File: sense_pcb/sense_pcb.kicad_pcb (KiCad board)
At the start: 2 copper layers, 31 parts, among them J1 Conn_02x06_Odd_Even, U1 DRV5053VAQDBZR, U10 DRV5053VAQDBZR, U11 DRV5053VAQDBZR, U12 DRV5053VAQDBZR, U13 DRV5053VAQDBZR, U14 4051, U15 DRV5053VAQDBZR, U16 DRV5053VAQDBZR, U17 DRV5053VAQDBZR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

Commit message: IC layout done
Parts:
- added J10, J11, J9: TEST_1P, SMD_Packages:1Pin, F.Cu at (226.6, 81.8)
- added J2: TEST_1P, SMD_Packages:1Pin, F.Cu at (241.1, 103.3)
- added J3: TEST_1P, SMD_Packages:1Pin, F.Cu at (240.7, 92.7)
- added J4: TEST_1P, SMD_Packages:1Pin, F.Cu at (216.1, 101.0)
- added J5: TEST_1P, SMD_Packages:1Pin, F.Cu at (208.3, 98.4)
- added J6: TEST_1P, SMD_Packages:1Pin, F.Cu at (225.4, 94.7)
- added J7: TEST_1P, SMD_Packages:1Pin, F.Cu at (233.1, 99.4)
- added J8: TEST_1P, SMD_Packages:1Pin, F.Cu at (252.2, 93.9)
- J1: value Conn_02x06_Odd_Even -> TEST_1P; footprint Pin_Headers:Pin_Header_Straight_2x06_Pitch2.54mm -> SMD_Packages:1Pin
- moved U21 112.4 mm to (258.7, 83.0), turned to 15 degrees
- moved U20 112.2 mm to (259.8, 91.3)
- moved U22 111.1 mm to (255.5, 75.2), turned to 30 degrees
- moved U19 110.4 mm to (258.7, 99.7), turned to 345 degrees
- moved U27 108.2 mm to (250.4, 68.5), turned to 45 degrees
- moved U8 107.0 mm to (255.5, 107.4), turned to 330 degrees
- moved U25 103.9 mm to (243.7, 63.4), turned to 60 degrees
- moved U23 102.9 mm to (248.2, 79.4), turned to 210 degrees
- moved U6 102.3 mm to (250.4, 114.1), turned to 315 degrees
- moved U24 98.2 mm to (235.9, 60.2), turned to 75 degrees
- moved U7 96.2 mm to (243.7, 119.3), turned to 300 degrees
- moved C2 95.8 mm to (241.7, 83.1), turned to 300 degrees
- moved U26 91.4 mm to (227.5, 59.0), turned to 90 degrees
- moved J1 89.2 mm to (237.1, 115.7), turned to 90 degrees
- moved U9 89.1 mm to (235.9, 122.5), turned to 285 degrees
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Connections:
- U14 pad 10: Net-(J1-Pad10) -> Net-(J10-Pad1)
- U14 pad 11: Net-(J1-Pad9) -> Net-(J3-Pad1)
- U14 pad 3: Net-(J1-Pad4) -> Net-(J9-Pad1)
- U14 pad 6: Net-(J1-Pad5) -> Net-(J4-Pad1)
- U14 pad 9: Net-(J1-Pad8) -> Net-(J7-Pad1)
- U23 pad 10: Net-(J1-Pad10) -> Net-(J10-Pad1)
- U23 pad 11: Net-(J1-Pad9) -> Net-(J3-Pad1)
- U23 pad 3: Net-(J1-Pad2) -> Net-(J11-Pad1)
- U23 pad 6: Net-(J1-Pad7) -> Net-(J5-Pad1)
- U23 pad 9: Net-(J1-Pad8) -> Net-(J7-Pad1)
- U5 pad 10: Net-(J1-Pad10) -> Net-(J10-Pad1)
- U5 pad 11: Net-(J1-Pad9) -> Net-(J3-Pad1)
- U5 pad 3: Net-(J1-Pad6) -> Net-(J8-Pad1)
- U5 pad 6: Net-(J1-Pad3) -> Net-(J2-Pad1)
- U5 pad 9: Net-(J1-Pad8) -> Net-(J7-Pad1)

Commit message: much smaller pads
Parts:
- J1, J10, J11, J2, J3, J4, J5, J6, J7, J8, J9: footprint SMD_Packages:1Pin -> Measurement_Points:Measurement_Point_Round-SMD-Pad_Small
- moved J5 33.3 mm to (240.3, 107.6)
- moved J10 29.8 mm to (251.0, 98.9)
- moved J9 28.2 mm to (244.1, 103.9)
- moved J11 26.8 mm to (246.3, 99.9)
- moved J4 26.5 mm to (240.2, 112.1)
- moved J6 24.2 mm to (245.3, 108.5)
- moved J7 16.5 mm to (249.1, 103.7)
- moved J3 16.3 mm to (253.9, 102.4)
- moved J8 14.9 mm to (250.2, 108.7)
- moved J2 11.2 mm to (244.8, 113.9)
- moved J1 2.10 mm to (238.0, 117.5)

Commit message: went over to Kicad 5.0, seems legit so far
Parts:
- removed C2, C3: C, Capacitors_SMD:C_1206_HandSoldering
- removed J10, J11, J8, J9: TEST_1P, Measurement_Points:Measurement_Point_Round-SMD-Pad_Small
- removed U10, U11, U12, U13, U15, U16, U17, U18, U19, U20, U21, U22, U24, U25, U26, U27: DRV5053VAQDBZR, digikey-footprints:SOT-23-3
- removed U14, U23: 4051, SMD_Packages:SO-16-N
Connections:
- J1 pad 1: VCC -> Net-(J1-Pad1)
- J2 pad 1: Net-(J2-Pad1) -> VCC
- J3 pad 1: Net-(J3-Pad1) -> GND
- J6 pad 1: GND -> Net-(J6-Pad1)
- U5 pad 10: Net-(J10-Pad1) -> Net-(J5-Pad1)
- U5 pad 11: Net-(J3-Pad1) -> Net-(J6-Pad1)
- U5 pad 3: Net-(J8-Pad1) -> Net-(J1-Pad1)
- U5 pad 6: Net-(J2-Pad1) -> Net-(J7-Pad1)
- U5 pad 9: Net-(J7-Pad1) -> Net-(J4-Pad1)

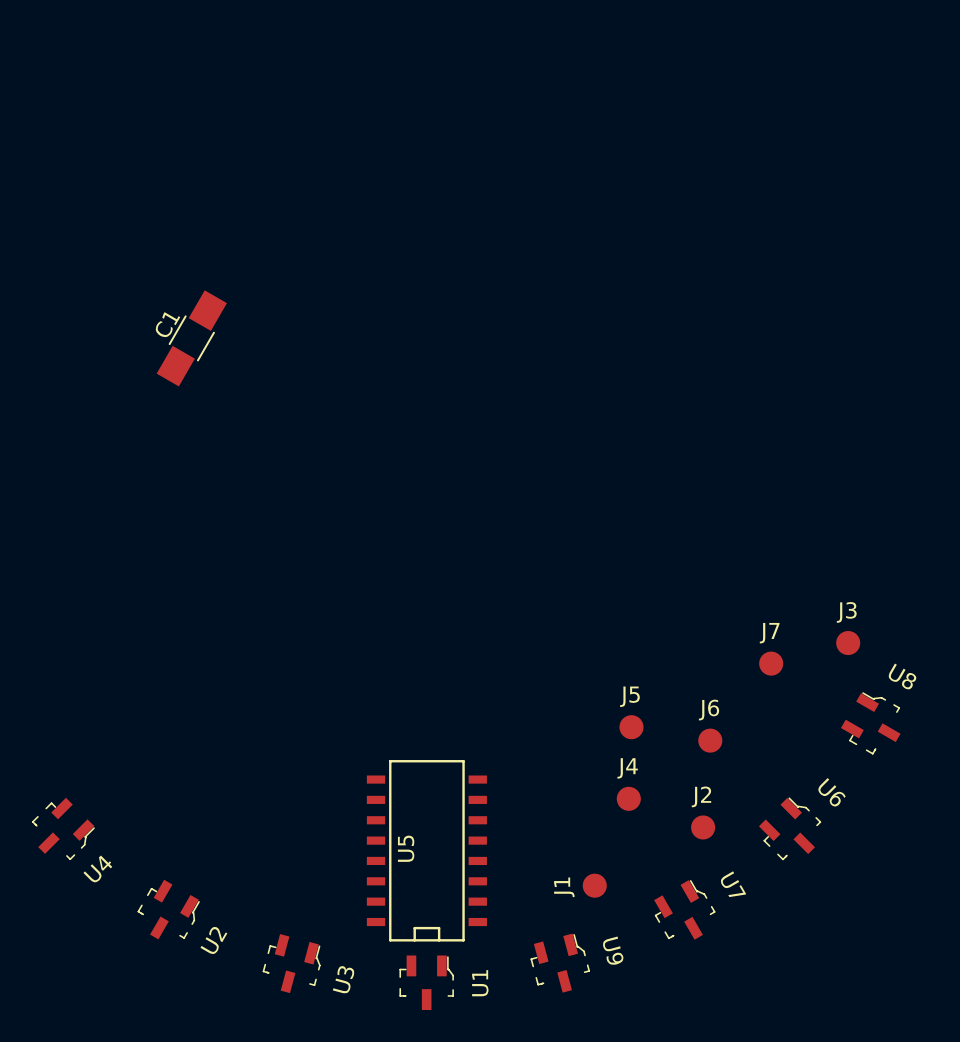
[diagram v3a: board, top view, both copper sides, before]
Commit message: layout with 8 sensors, no routing yet
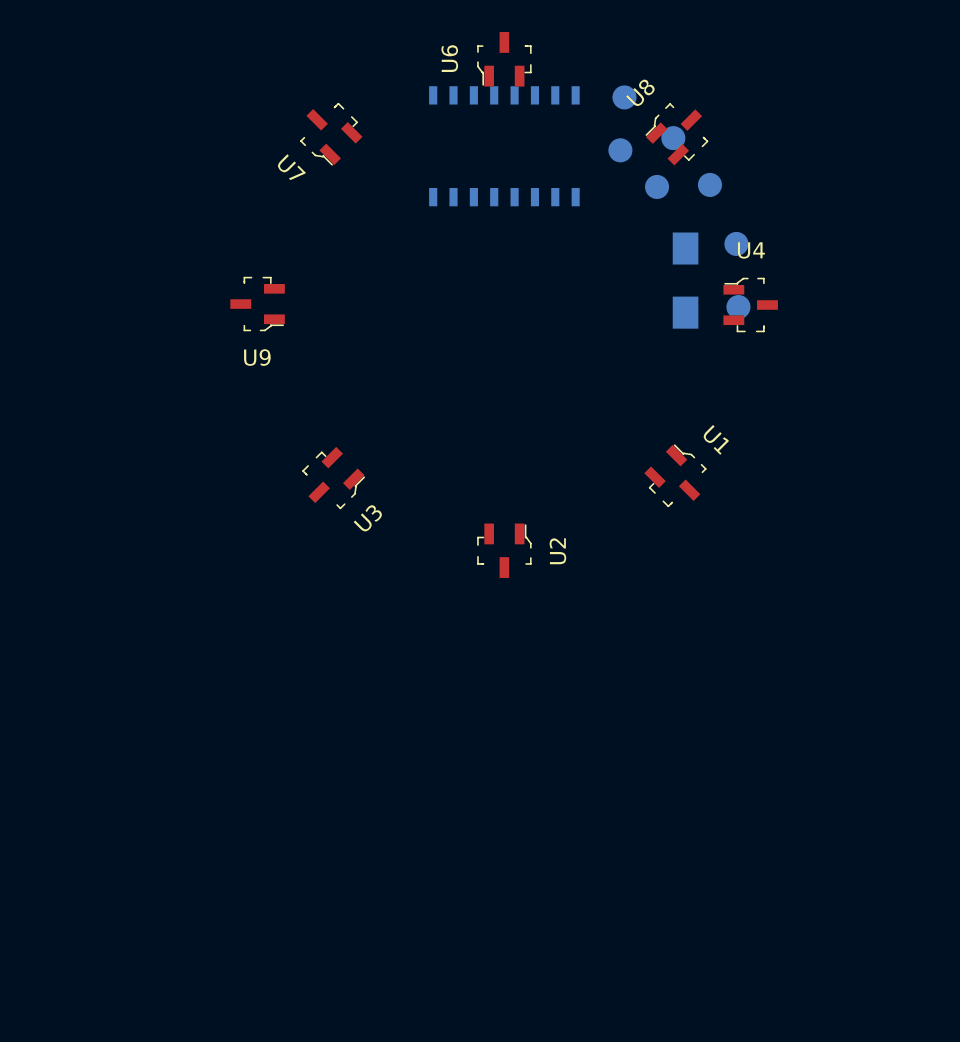
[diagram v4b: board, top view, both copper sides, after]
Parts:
- added G***: LOGO, graphics:layout.35mm, F.Cu at (232.4, 81.3)
- C1, J1, J2, J3, J4, J5, J6, J7, U5: moved to B.Cu
- moved U4 54.1 mm to (247.8, 81.3), turned to 0 degrees
- moved U7 53.6 mm to (221.5, 70.5), turned to 135 degrees
- moved U6 51.4 mm to (232.4, 65.9), turned to 90 degrees
- moved J1 46.9 mm to (243.0, 70.9), turned to 270 degrees
- moved U9 45.4 mm to (217.0, 81.2), turned to 180 degrees
- moved U5 44.2 mm to (232.4, 71.4), turned to 0 degrees
- moved U8 38.9 mm to (243.3, 70.5), turned to 45 degrees
- moved J4 38.6 mm to (245.2, 73.8)
- moved J6 37.3 mm to (239.6, 71.6)
- moved J7 36.5 mm to (239.9, 68.3)
- moved J2 36.5 mm to (246.9, 77.5)
- moved U1 35.2 mm to (243.2, 92.1), turned to 315 degrees
- moved J5 33.7 mm to (241.9, 73.9)
- moved C1 31.0 mm to (243.7, 79.8), turned to 270 degrees
- moved U2 30.9 mm to (232.4, 96.6), turned to 270 degrees
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
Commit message: routing complete
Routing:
- net VCC: track 0.00 -> 106.9 mm, vias 0 -> 3
- net GND: track 0.00 -> 97.9 mm, vias 0 -> 2
- net Net-(U2-Pad2): track 0.00 -> 29.7 mm, vias 0 -> 1
- net Net-(U1-Pad2): track 0.00 -> 29.3 mm, vias 0 -> 1
- net Net-(U4-Pad2): track 0.00 -> 22.6 mm, vias 0 -> 1
- net Net-(U3-Pad2): track 0.00 -> 20.7 mm, vias 0 -> 1
- net Net-(U5-Pad1): track 0.00 -> 15.9 mm, vias 0 -> 1
- net Net-(J1-Pad1): track 0.00 -> 14.4 mm
- net Net-(U5-Pad5): track 0.00 -> 12.4 mm, vias 0 -> 1
- net Net-(U5-Pad2): track 0.00 -> 10.6 mm, vias 0 -> 1
- net Net-(J4-Pad1): track 0.00 -> 9.50 mm
- net Net-(J5-Pad1): track 0.00 -> 8.09 mm
- net Net-(J6-Pad1): track 0.00 -> 8.02 mm
- net Net-(J7-Pad1): track 0.00 -> 7.51 mm
- net Net-(U5-Pad4): track 0.00 -> 5.20 mm, vias 0 -> 1

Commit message: adds v1 manufacturing files as sent to dirtypcbs.com
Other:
- board outline added: 35.6 x 35.6 mm
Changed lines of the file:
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@@
   (general
     (thickness 1.6)
-    (drawings 0)
+    (drawings 1)
     (tracks 159)
     (zones 0)
@@
       (xy -0.175598 -17.33005) (xy 0.565177 -17.32163)) (layer Eco1.User) (width 0.01))
   )
+  (gr_circle (center 232.41 81.28) (end 248.793 88.265) (layer Edge.Cuts) (width 0.2))
   (segment (start 233.36 95.563) (end 242.062 89.535) (width 0.45) (layer F.Cu) (net 1))
   (segment (start 242.062 89.535) (end 243.153827 90.680324) (width 0.45) (layer F.Cu) (net 1))

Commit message: adds sensor test
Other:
- outline, holes or cut-outs redrawn
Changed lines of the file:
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@@
-(kicad_pcb (version 20171130) (host pcbnew 5.0.2-bee76a0~70~ubuntu18.04.1)
+(kicad_pcb (version 4) (host pcbnew 4.0.7-e2-6376~58~ubuntu16.04.1)
   (general
+    (links 34)
+    (no_connects 0)
+    (area 210.093523 59.031523 254.692477 103.528476)
     (thickness 1.6)
-    (drawings 1)
+    (drawings 2)
     (tracks 159)
     (zones 0)
@@
   )
   (setup
-    (last_trace_width 0.45)
+    (last_trace_width 0.25)
     (user_trace_width 0.45)
     (user_trace_width 0.5)
@@
       (layerselection 0x00030_80000001)
       (usegerberextensions false)
-      (usegerberattributes false)
-      (usegerberadvancedattributes false)
-      (creategerberjobfile false)
       (excludeedgelayer true)
       (linewidth 0.100000)
@@
       (hpglpennumber 1)
       (hpglpenspeed 20)
-      (hpglpendiameter 15.000000)
+      (hpglpendiameter 15)
+      (hpglpenoverlay 2)
       (psnegative false)
       (psa4output false)
@@
     (at 232.41 81.28)
     (fp_text reference G*** (at 0 0) (layer F.SilkS) hide
-      (effects (font (size 1.524 1.524) (thickness 0.3)))
+      (effects (font (thickness 0.3)))
     )
     (fp_text value LOGO (at 0.75 0) (layer F.SilkS) hide
-      (effects (font (size 1.524 1.524) (thickness 0.3)))
+      (effects (font (thickness 0.3)))
     )
     (fp_poly (pts (xy 0.170867 -1.017051) (xy 0.328859 -0.977285) (xy 0.477313 -0.913687) (xy 0.613603 -0.828223)
@@
       (xy -0.175598 -17.33005) (xy 0.565177 -17.32163)) (layer Eco1.User) (width 0.01))
   )
+  (gr_circle (center 232.41508 81.28) (end 236.01172 82.45348) (layer Edge.Cuts) (width 0.15))
   (gr_circle (center 232.41 81.28) (end 248.793 88.265) (layer Edge.Cuts) (width 0.2))
   (segment (start 233.36 95.563) (end 242.062 89.535) (width 0.45) (layer F.Cu) (net 1))
